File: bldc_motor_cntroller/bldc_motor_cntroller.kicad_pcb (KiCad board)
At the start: 4 copper layers, 58 x 50 mm, 144 parts, among them J1 SM06B-SRSS-TB, J10 MR30PW-M 15A (30A), J2 Conn_01x18, J5 0475900001, J6 TC2030 Tag-connect, J7 SH-SM02B-SRSS, J8 XT60, J9 XT60, Q1 CSD18540Q5B, Q2 CSD18540Q5B, Q3 CSD18540Q5B, Q4 CSD18540Q5B, Q5 CSD18540Q5B, Q6 CSD18540Q5B, Q7 CSD18540Q5B, Q8 CSD18540Q5B, SW1 SW_Push, SW2 SW_Push, U1 TCAN332GDCNT, U2 TLV75733PDBV, U3 LM5109BSD, U4 DRV8301DCAR, U5 STM32F405RGTx, Y1 8MHz

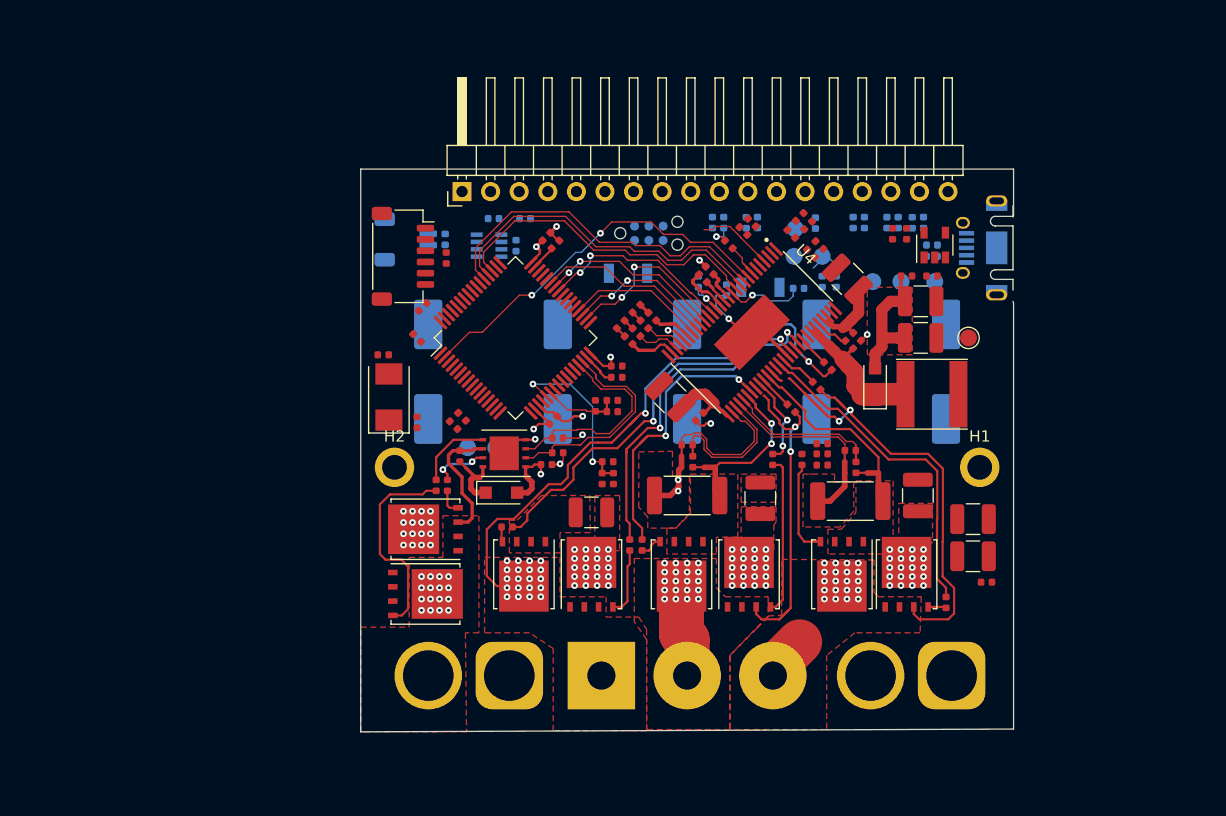
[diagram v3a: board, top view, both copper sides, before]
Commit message: finished routing. DRC check pass with some known voilations.
Signed-off-by: azmat bilal <azmat.bilal@outlook.com>
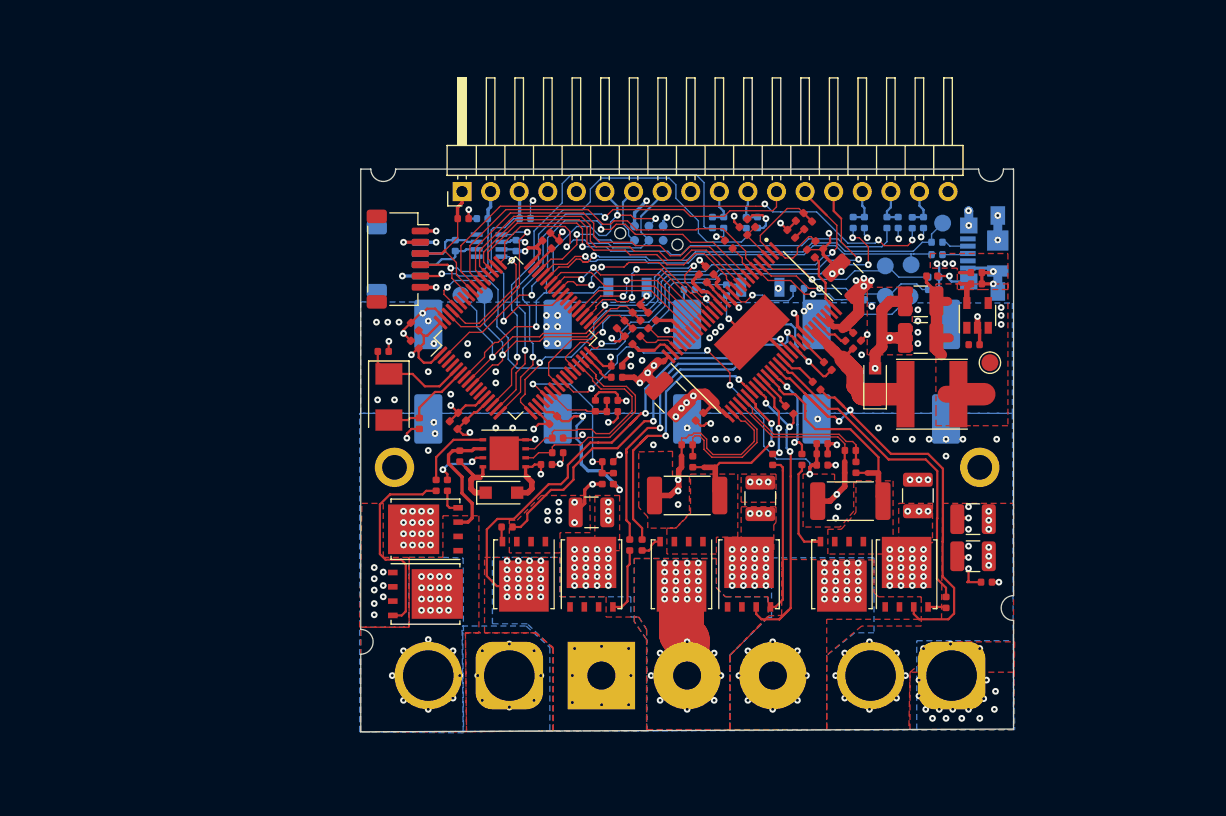
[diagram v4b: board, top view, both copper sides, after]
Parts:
- removed J7: SH-SM02B-SRSS, Connector_JST:JST_SH_SM02B-SRSS-TB_1x02-1MP_P1.00mm_Horizontal
- removed TP1: TestPoint, TestPoint:TestPoint_Pad_D1.5mm
- added HS1: Heatsink, bldc_motor_cntroller:heatsink14x14x6, B.Cu at (138.6, 89.7)
- added HS2: Heatsink, bldc_motor_cntroller:heatsink14x14x6, B.Cu at (109.2, 89.7)
- added HS3: Heatsink, bldc_motor_cntroller:heatsink14x14x6, B.Cu at (123.8, 89.7)
- added J3: SM04B-SRSS-TB(LF)(SN), Connector_JST:JST_SH_SM04B-SRSS-TB_1x04-1MP_P1.00mm_Horizontal, B.Cu at (103.3, 58.0)
- J1: value SM06B-SRSS-TB -> SM06B-SRSS-TB(LF)(SN)
- J5: value 0475900001 -> 0473460001; footprint Connector_USB:USB_Micro-AB_Molex_47590-0001 -> Connector_USB:USB_Micro-B_Molex_47346-0001
- moved TP9 13.6 mm to (111.0, 61.2)
- moved TP8 13.6 mm to (108.9, 61.2)
- moved R27 12.0 mm to (150.9, 60.7), turned to 0 degrees
- moved TP5 10.9 mm to (148.8, 61.3)
- moved TP6 10.0 mm to (146.6, 61.3)
- moved R25 8.66 mm to (150.9, 59.6), turned to 0 degrees
- moved C36 8.56 mm to (154.5, 65.6), turned to 0 degrees
- moved C19 8.21 mm to (154.7, 59.2), turned to 0 degrees
- moved TP3 8.09 mm to (151.7, 54.8)
- moved C18 7.63 mm to (154.7, 60.2), turned to 0 degrees
- moved U2 7.31 mm to (154.8, 63.0)
- moved C56 6.98 mm to (102.0, 66.2), turned to 180 degrees
- moved C57 6.89 mm to (105.2, 72.6), turned to 90 degrees
- moved TP4 5.66 mm to (146.6, 58.6)
- moved R5 3.81 mm to (109.1, 54.4), turned to 180 degrees
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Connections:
- J5 pad 1: VBUS -> (no net)
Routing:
- net VDD: track 12.4 -> 125.6 mm, vias 4 -> 19
- net GND: track 50.3 -> 130.8 mm, vias 12 -> 135
- net /Microcontroller Interface/nFAULT: track 0.80 -> 50.6 mm, vias 0 -> 1
- net /I/O Interface/GPIO_8: track 0.00 -> 48.9 mm, vias 0 -> 3
- net /I/O Interface/GPIO_4: track 0.00 -> 44.0 mm, vias 0 -> 2
- net /I/O Interface/GPIO_2: track 0.00 -> 43.5 mm, vias 0 -> 1
- net /I/O Interface/GPIO_5: track 0.00 -> 42.8 mm, vias 0 -> 2
- net /I/O Interface/GPIO_7: track 0.00 -> 42.6 mm, vias 0 -> 1
- net /I/O Interface/GPIO_3: track 0.00 -> 41.9 mm, vias 0 -> 2
- net /I/O Interface/GPIO_1: track 0.00 -> 40.6 mm, vias 0 -> 1
- net /I/O Interface/BOOT0: track 0.00 -> 40.5 mm, vias 0 -> 1
- net /I/O Interface/USB_DM: track 0.00 -> 39.3 mm, vias 0 -> 1
- net /I/O Interface/GPIO_6: track 0.00 -> 37.8 mm, vias 0 -> 3
- net /I/O Interface/USB_DP: track 0.00 -> 37.6 mm, vias 0 -> 1
- net /I/O Interface/DEBUG_nRESET: track 0.00 -> 37.0 mm, vias 0 -> 3
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- added copper zone on F.Cu, net +5V
- added copper zone on In2.Cu, net +5V
- added copper zone on B.Cu, net /Motor Driver/SH_A
- added copper zone on B.Cu, net /Motor Driver/SH_B
- added copper zone on B.Cu, net /Motor Driver/SH_C
- added copper zone on B.Cu, net GND
- added copper zone on B.Cu, net Net-(C16-Pad2)
- added copper zone on B.Cu, net VDC
- added copper zone on F.Cu, net VDD
- added copper zone on In2.Cu, net VDD
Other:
- outline, holes or cut-outs redrawn
- net class HV: clearance 0.3 -> 0.28

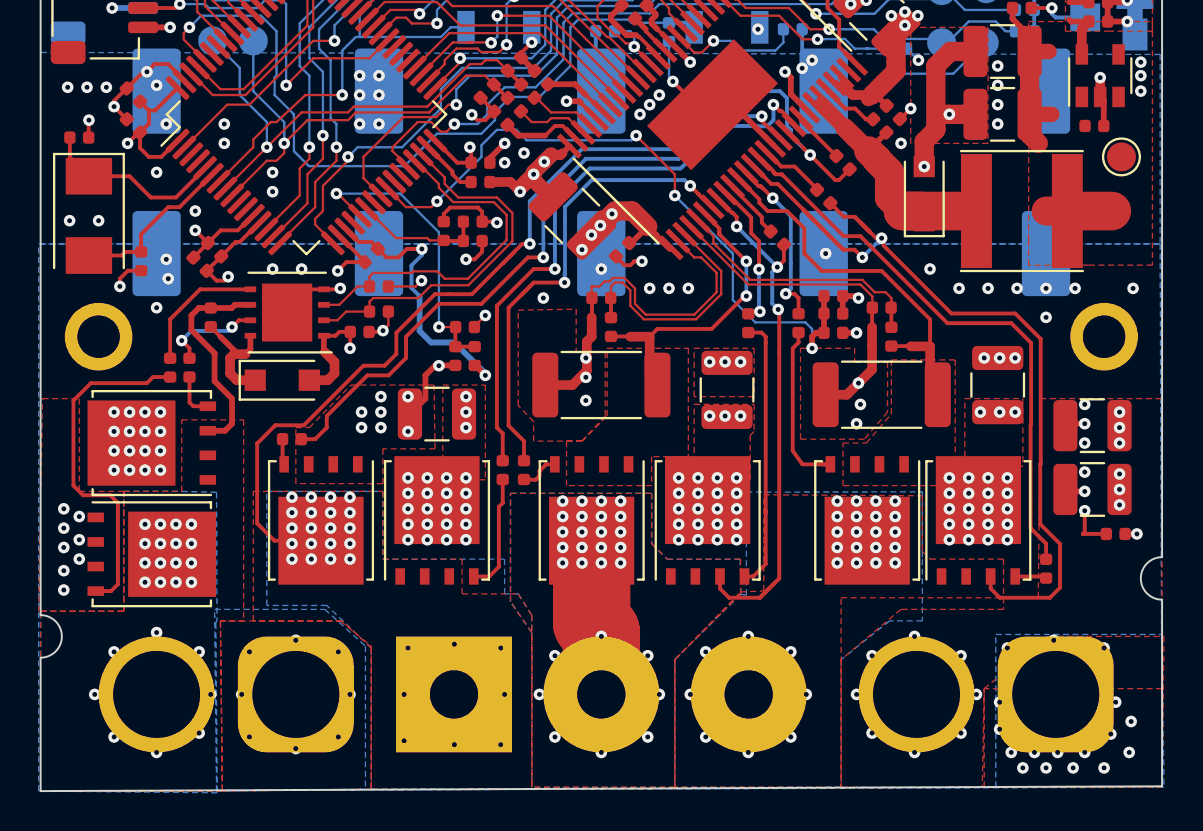
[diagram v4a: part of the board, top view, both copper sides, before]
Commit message: improved assembly documentation
Signed-off-by: azmat bilal <azmat.bilal@outlook.com>
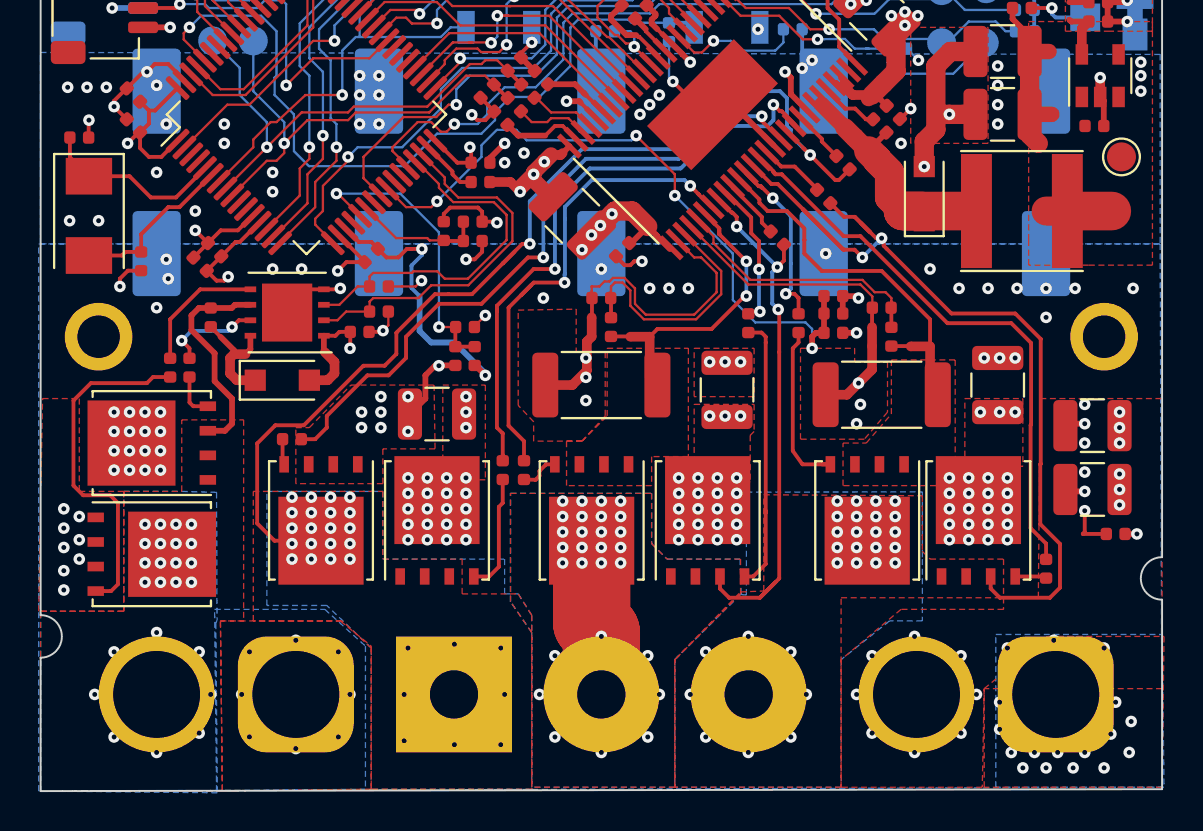
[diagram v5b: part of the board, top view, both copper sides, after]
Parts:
- C14: value 270pF 50V -> 270pF
- C16: value 100nF 50V -> 100nF
- C37, C41: value 2200PF 50V -> 2200pF
- C38: value 82pF 50V 5% -> 82pF
- C39: value 270pF 50V 5% -> 270pF
- C40: value 15nF 50V -> 15nF
- C45, C46: value 2200PF 50V -> 2200PF
- SW1, SW2: value SW_Push -> B3U-1000P-B
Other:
- outline, holes or cut-outs redrawn
